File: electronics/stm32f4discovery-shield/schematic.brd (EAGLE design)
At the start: 100 x 80 mm, 1 part

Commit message: Iniciando o routing.
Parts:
- added C1: 104, SparkFun-Capacitors:CAP-PTH-SMALL-KIT
- added C2, C3: (no value), SparkFun-Capacitors:CAP-PTH-SMALL-KIT
- added ESC, JP1: (no value), con-lstb:MA03-2
- added I2C1_ESC, I2C3_IMU, SPI1, US2, US5_SONAR, US6: RJ11-2L-B, con-tycoelectronics:RJ11-NO_SHIELD
- added IC1: MAX3468CPA, maxim:DIL08
- added IC2: (no value), SparkFun-PowerIC:TO-220-ALT
- added IC3, IC4: LM340H-12, linear:TO220H
- added ISP1: AVRISP-6, adafruit:AVRISP
- added J1: POWER_JACKSLT, SparkFun-Connectors:POWER_JACK_SLOT
- added JP2, JP3: (no value), SparkFun-Passives:1X02
- added JP4: (no value), jumper:JP2
- added LED1, LED2, LED_PWR: (no value), adafruit:LED5MM
- added Q1: BC548, transistor-npn:TO92-EBC
- added R1, R3: (no value), adafruit:M1206
- added R10, R4, R5, R6, R7, R8, R9: (no value), adafruit:0204/7
- added R2: (no value), rcl:0204V
- added RECV, SV1, SV2, SV3: (no value), con-lstb:MA03-1
- added SJ1: (no value), jumper:SJ_2W
- added SRVO1, SRVO2: (no value), SparkFun-Connectors:MOLEX-1X4
- added U$2: JYMCU_LOGIC_LEVEL_CONVERTER, provant_custom:JYMCU_LOGIC_LEVEL_SHIFTER_DIP
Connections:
- new net 3.3V: I2C1_ESC.1, I2C3_IMU.1, R1.2, R3.2, U$1.P$55, U$1.P$56, U$2.3V3, US2.1, US5_SONAR.1, US6.1
- new net 5V: C1.1, I2C1_ESC.2, I2C3_IMU.2, IC1.8, ISP1.2, JP4.2, R10.1, R2.2, R4.2, R9.1, RECV.2, SPI1.2, SV1.2, SV2.2, SV3.2, U$1.P$53, U$1.P$54, U$2.5V, US2.2, US5_SONAR.2, US6.2
- new net 5V_REG: C3.1, IC2.OUT, JP4.1
- new net D+/TX: IC1.6, JP3.2, SRVO1.3, SRVO2.3
- new net D-/RX: IC1.7, JP2.2, SRVO1.4, SRVO2.4
- new net GND: C1.2, C2.2, C3.2, ESC.1, ESC.2, I2C1_ESC.5, I2C1_ESC.6, I2C3_IMU.5, I2C3_IMU.6, IC1.5, IC2.GND, ISP1.6, J1.GND@1, J1.GND@2, LED_PWR.K, Q1.E, R6.2, R8.2, RECV.3, SPI1.6, SRVO1.1, SRVO2.1, SV1.3, SV2.3, SV3.3, U$1.P$1, U$1.P$100, U$1.P$2, U$1.P$23, U$1.P$49, U$1.P$5, U$1.P$50, U$1.P$51, U$1.P$52, U$1.P$99, U$2.GND1, U$2.GND2, US2.5, US2.6, US5_SONAR.5, US5_SONAR.6, US6.5, US6.6
- new net N$1: JP1.5, U$2.DL
- new net N$2: JP1.6, U$2.CL
- new net N$3: Q1.C, R2.1, SJ1.3
- new net N$4: LED_PWR.A, R4.1
- new net N$5: LED1.A, R9.2
- new net N$6: IC3.2, R5.1, R6.1
- new net N$7: LED2.A, R10.2
- new net N$8: IC4.2, R7.2, R8.1
- new net PA2/USART2_TX: U$1.P$14, US2.3
- new net PA3/USART2_RX: U$1.P$13, US2.4
- new net PA8/I2C3_SCL: JP1.4, U$1.P$93
- new net PB0/PWM: LED2.K
- new net PB1/PWM: LED1.K
- new net PB3/SPI1_SCK: ISP1.3, SPI1.5, U$1.P$78
- new net PB4/SPI1_MISO: ISP1.1, SPI1.4, U$1.P$75
- new net PB5/SPI1_MOSI: ISP1.4, SPI1.3, U$1.P$76
- new net PB6/USART1_TX: IC1.4, JP3.1, U$1.P$73
- new net PB7/USART1_RX: IC1.1, JP2.1, U$1.P$74
- new net PB8/I2C1_SCL: U$1.P$69, U$2.BL
- new net PB9/I2C1_SDA: U$1.P$70, U$2.AL
- new net PC10/USART3_TX: U$1.P$87, US5_SONAR.3
- new net PC11/USART3_RX: SJ1.2, U$1.P$88
- new net PC6/USART6_TX: U$1.P$97, US6.3
- new net PC7/USART6_RX: U$1.P$98, US6.4
- new net PC9/I2C3_SDA: JP1.3, U$1.P$96
- new net PE11/PWM: SV3.1
- new net PE13/PWM: SV2.1
- new net PE14/PWM: SV1.1
- new net PE2: IC1.2, IC1.3, U$1.P$65
- new net PE9/PWM: RECV.1
- new net SCL1: ESC.5, ESC.6, I2C1_ESC.4, U$2.BH
- new net SCL2: I2C3_IMU.4, JP1.2, R3.1, U$2.CH
- new net SDA1: ESC.3, ESC.4, I2C1_ESC.3, U$2.AH
- new net SDA2: I2C3_IMU.3, JP1.1, R1.1, U$2.DH
- new net SONAR_RX: Q1.B, SJ1.1, US5_SONAR.4
- new net SRVO1_PWR: IC4.3, R7.1, SRVO1.2
- new net SRVO2_PWR: IC3.3, R5.2, SRVO2.2
- new net VCC: C2.1, IC2.IN, IC3.1, IC4.1, J1.PWR, JP4.3
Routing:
- net 5V: track 0.00 -> 88.7 mm
- net D+/TX: track 0.00 -> 70.1 mm
- net D-/RX: track 0.00 -> 57.9 mm
- net SCL2: track 0.00 -> 43.1 mm
- net SDA2: track 0.00 -> 41.6 mm
- net PB7/USART1_RX: track 0.00 -> 35.4 mm
- net PB3/SPI1_SCK: track 0.00 -> 31.5 mm, vias 0 -> 1
- net PB4/SPI1_MISO: track 0.00 -> 29.7 mm
- net SCL1: track 0.00 -> 28.4 mm
- net 3.3V: track 0.00 -> 26.4 mm
- net SDA1: track 0.00 -> 26.3 mm
- net PC10/USART3_TX: track 0.00 -> 26.3 mm
- net PB6/USART1_TX: track 0.00 -> 24.5 mm
- net SONAR_RX: track 0.00 -> 23.3 mm
- net PE2: track 0.00 -> 23.2 mm
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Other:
- board size 100 x 80 mm -> 103.8 x 110.5 mm

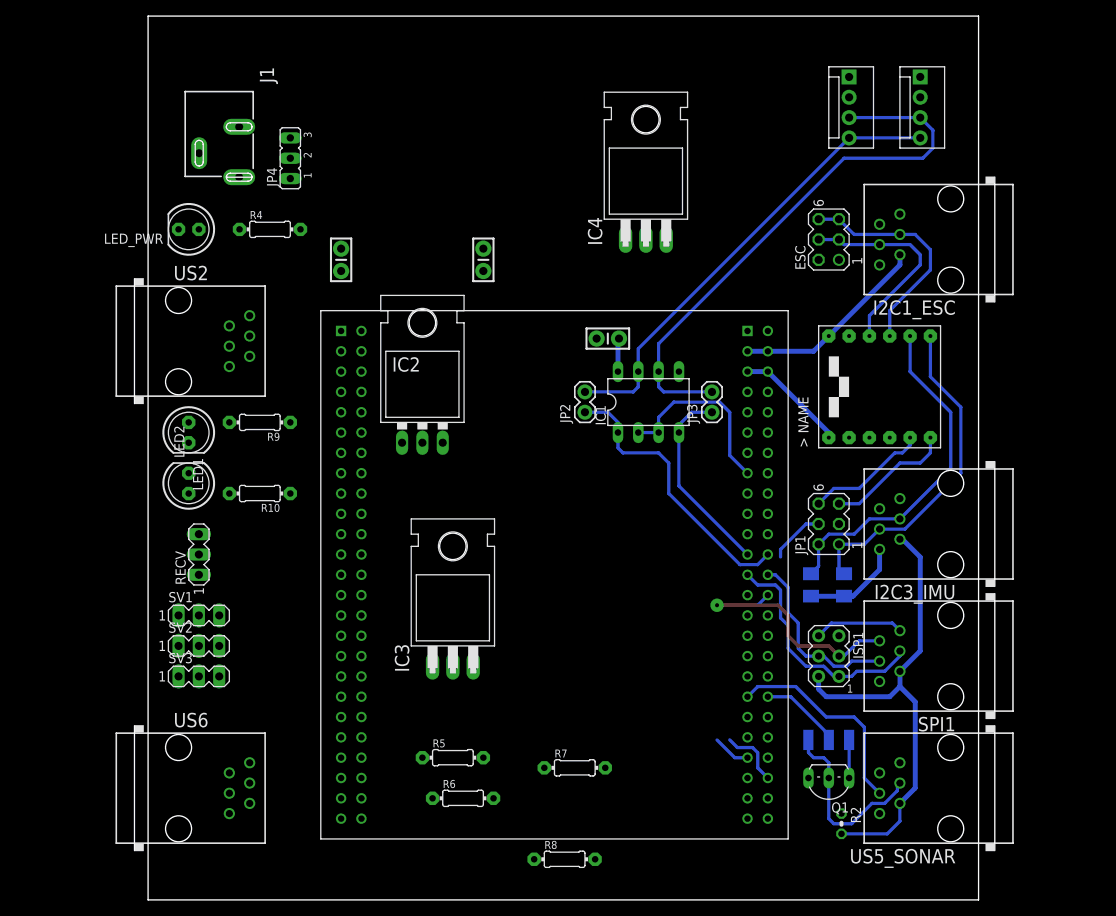
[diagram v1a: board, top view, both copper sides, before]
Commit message: Primeira versao para fabricacao da placa STM32 Discovery.
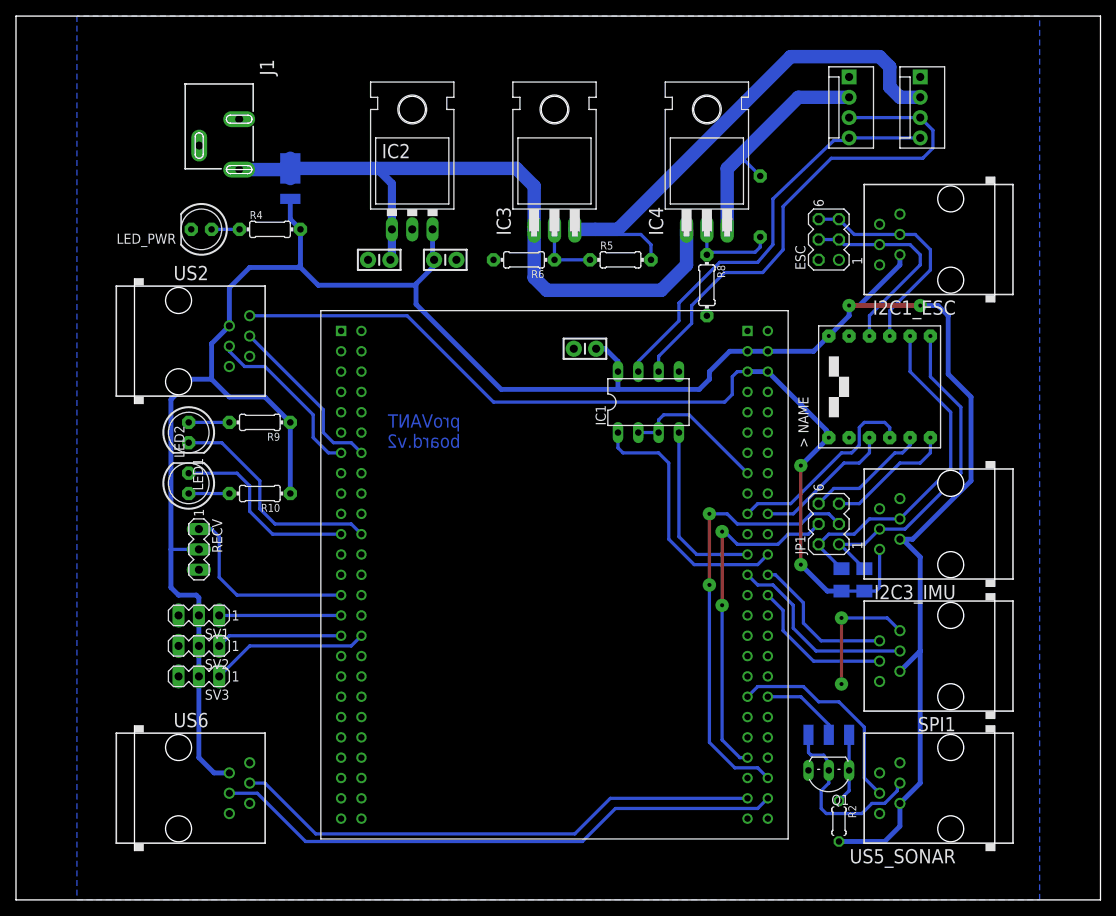
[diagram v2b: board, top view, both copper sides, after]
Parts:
- removed ISP1: AVRISP-6, adafruit:AVRISP
- removed JP2, JP3: (no value), SparkFun-Passives:1X02
- removed JP4: (no value), jumper:JP2
- added SJ3: (no value), SparkFun-Passives:SJ_2W
- R2: device rcl:0204V -> rcl:0204/5
- moved R8 73.9 mm to (69.8, 76.8), turned to 270 degrees
- moved R7 73.9 mm to (76.5, 86.7), flipped to the bottom, turned to 270 degrees
- moved R6 67.7 mm to (47.0, 80.0), turned to 180 degrees
- moved R5 65.7 mm to (59.1, 80.0)
- moved IC3 56.1 mm to (50.8, 94.0)
- moved IC2 26.7 mm to (33.0, 87.6)
- moved IC4 7.73 mm to (69.8, 94.0)
- moved C2 4.76 mm to (28.9, 80.0), turned to 180 degrees
- moved C3 4.76 mm to (37.1, 80.0), turned to 0 degrees
- moved R3 3.86 mm to (86.7, 40.0)
- moved C1 3.13 mm to (54.6, 68.9)
- moved R1 2.62 mm to (89.5, 40.0)
- moved LED_PWR 1.59 mm to (6.67, 83.8)
- moved J1 0.95 mm to (14.0, 105.1)
- moved Q1 0.95 mm to (85.1, 14.9)
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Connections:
- removed net 5V_REG: C3.1, IC2.OUT, JP4.1
- net 3.3V: no longer I2C1_ESC.1, US5_SONAR.1, US6.1
- net 5V: now also C3.1, IC2.OUT, SJ3.3; no longer ISP1.2, JP4.2
- net D+/TX: no longer JP3.2
- net D-/RX: no longer JP2.2
- net GND: no longer ISP1.6
- net PB0/PWM: now also LED1.K, U$1.P$22; no longer LED2.K
- net PB1/PWM: now also LED2.K, U$1.P$21; no longer LED1.K
- net PB3/SPI1_SCK: now also SPI1.3; no longer ISP1.3, SPI1.5
- net PB4/SPI1_MISO: no longer ISP1.1
- net PB5/SPI1_MOSI: now also SPI1.5; no longer ISP1.4, SPI1.3
- net PB6/USART1_TX: no longer JP3.1
- net PB7/USART1_RX: no longer JP2.1
- net PE11/PWM: now also SV1.1, U$1.P$29; no longer SV3.1
- net PE13/PWM: now also U$1.P$31
- net PE14/PWM: now also SV3.1, U$1.P$32; no longer SV1.1
- net PE9/PWM: now also U$1.P$27
- net VCC: now also SJ3.1, SJ3.2; no longer JP4.3
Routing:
- net 5V: track 88.7 -> 317.6 mm, vias 0 -> 2
- net 3.3V: track 26.4 -> 117.6 mm, vias 0 -> 2
- net VCC: track 0.00 -> 90.7 mm
- net PC7/USART6_RX: track 0.00 -> 72.0 mm
- net SRVO2_PWR: track 0.00 -> 68.4 mm
- net PC6/USART6_TX: track 0.00 -> 66.7 mm
- net PC9/I2C3_SDA: track 7.85 -> 55.5 mm, vias 0 -> 2
- net SRVO1_PWR: track 0.00 -> 38.9 mm
- net PA8/I2C3_SCL: track 11.8 -> 43.9 mm, vias 0 -> 2
- net PB0/PWM: track 0.00 -> 28.4 mm
- net PB8/I2C1_SCL: track 0.00 -> 25.3 mm
- net PE9/PWM: track 0.00 -> 24.2 mm
- net PB1/PWM: track 0.00 -> 24.1 mm
- net PA2/USART2_TX: track 0.00 -> 21.7 mm
- net PA3/USART2_RX: track 0.00 -> 21.5 mm
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- added copper zone on layer 16, net GND
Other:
- board size 103.8 x 110.5 mm -> 135.6 x 110.5 mm
- board text added: "proVANT board.v2"

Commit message: Adicionadas algumas correcoes.
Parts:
- moved R5 1.91 mm to (57.1, 80.0)
- renumbered U$2 to LVL
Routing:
- net GND: track 16.2 -> 57.0 mm, vias 2 -> 4
- net SRVO2_PWR: track 68.4 -> 61.8 mm
- net N$6: track 8.25 -> 6.35 mm
